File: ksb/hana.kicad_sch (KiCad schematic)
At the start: 20 parts, among them Q6 Q_PNP, U4 X850744-001

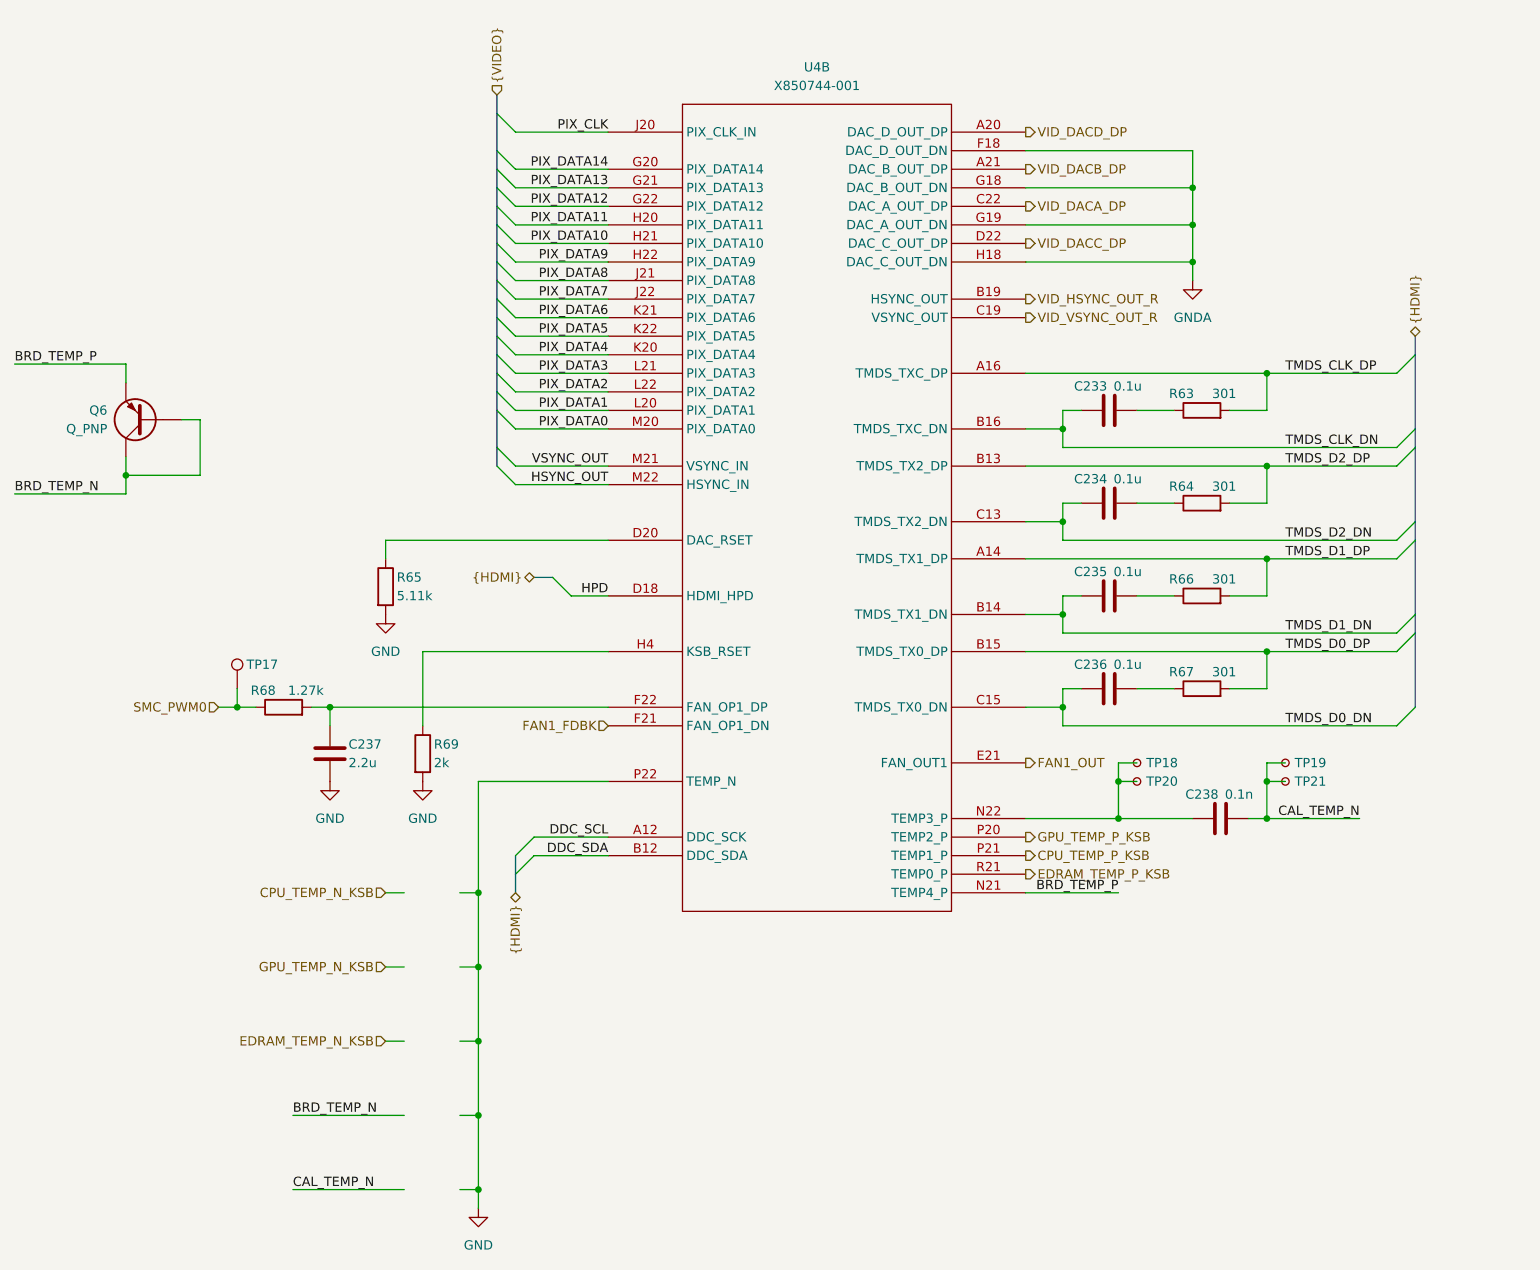
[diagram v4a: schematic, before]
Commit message: Nand Flash, Sata Connectors and removing (hopefully) unnecessary things
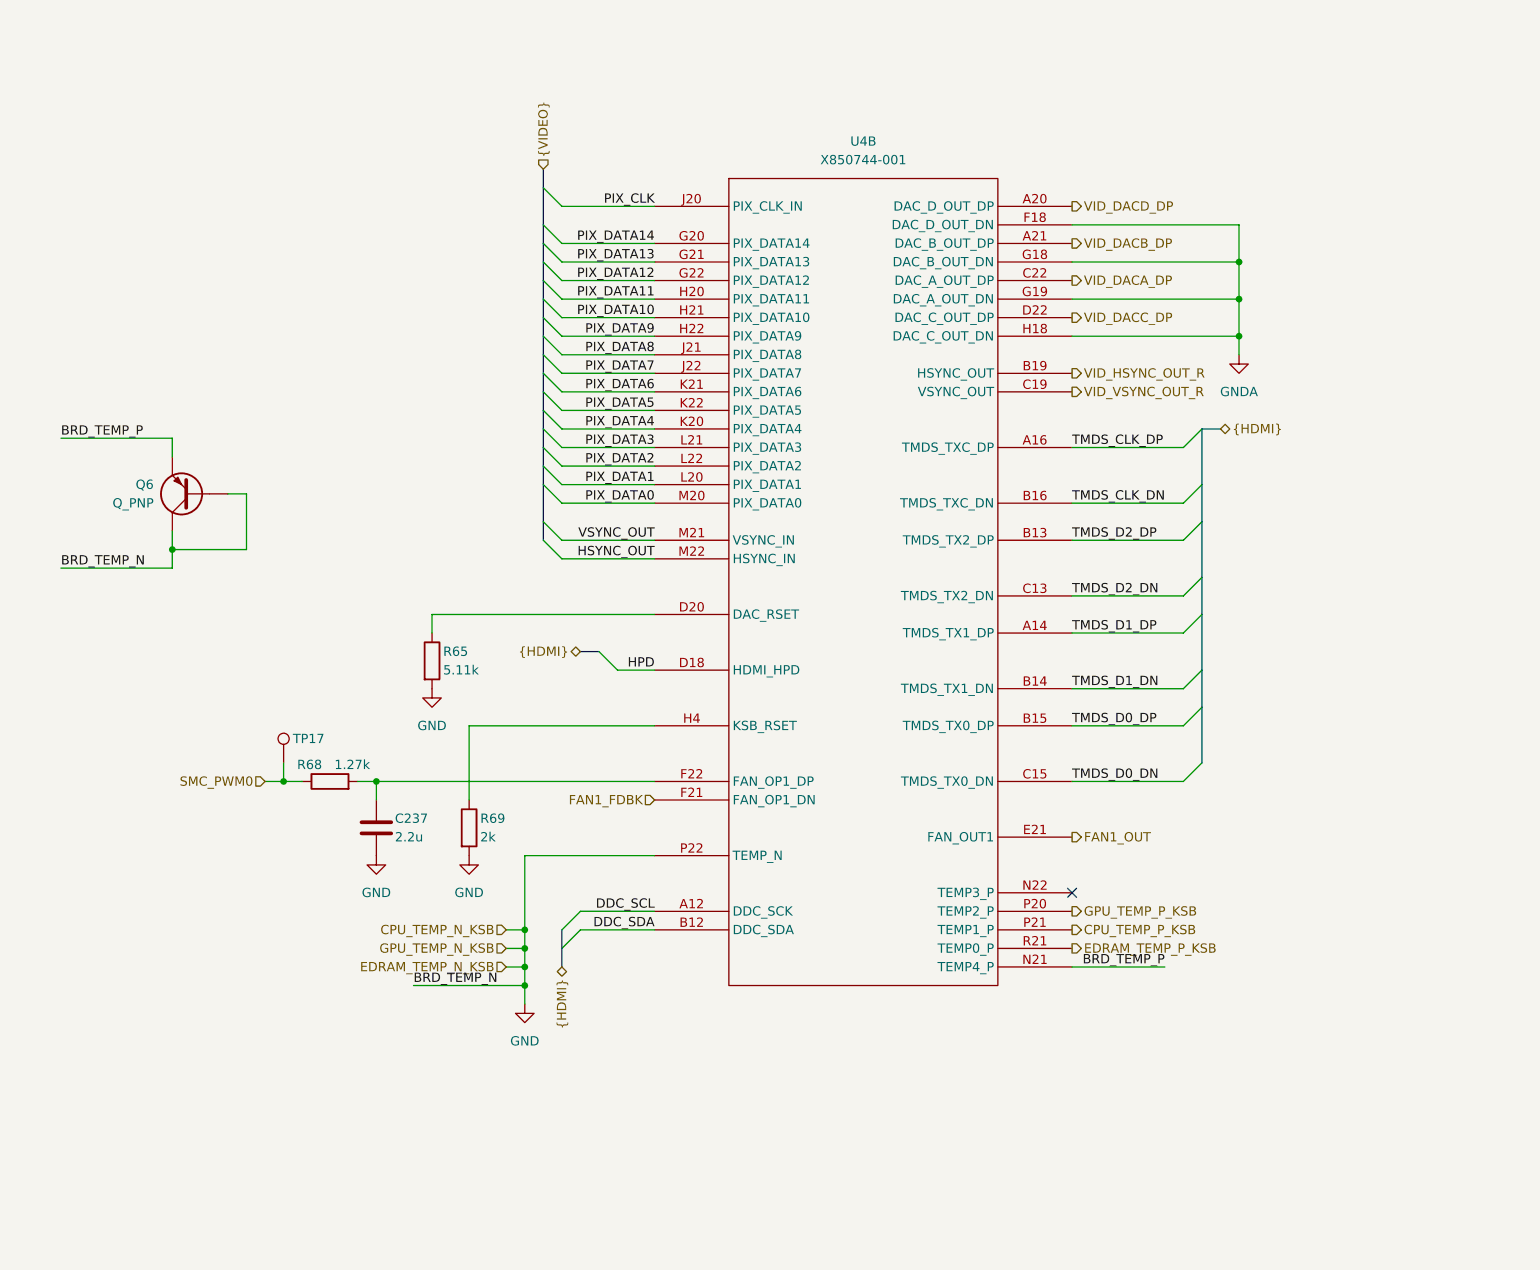
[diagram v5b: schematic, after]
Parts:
- removed C233, C234, C235, C236: 0.1u, symbol Device:C
- removed C238: 0.1n, symbol Device:C
- removed R63, R64, R66, R67: 301, symbol Device:R
- removed TP18, TP19, TP20, TP21: TestPoint_Small, symbol Connector:TestPoint_Small
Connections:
- net BRD_TEMP_N is gone; now on net GND: Q6.B, Q6.C
- no-connect marks 0 -> 1
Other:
- moved on the sheet: C237, Q6, R65, R68, R69, TP17, U4B

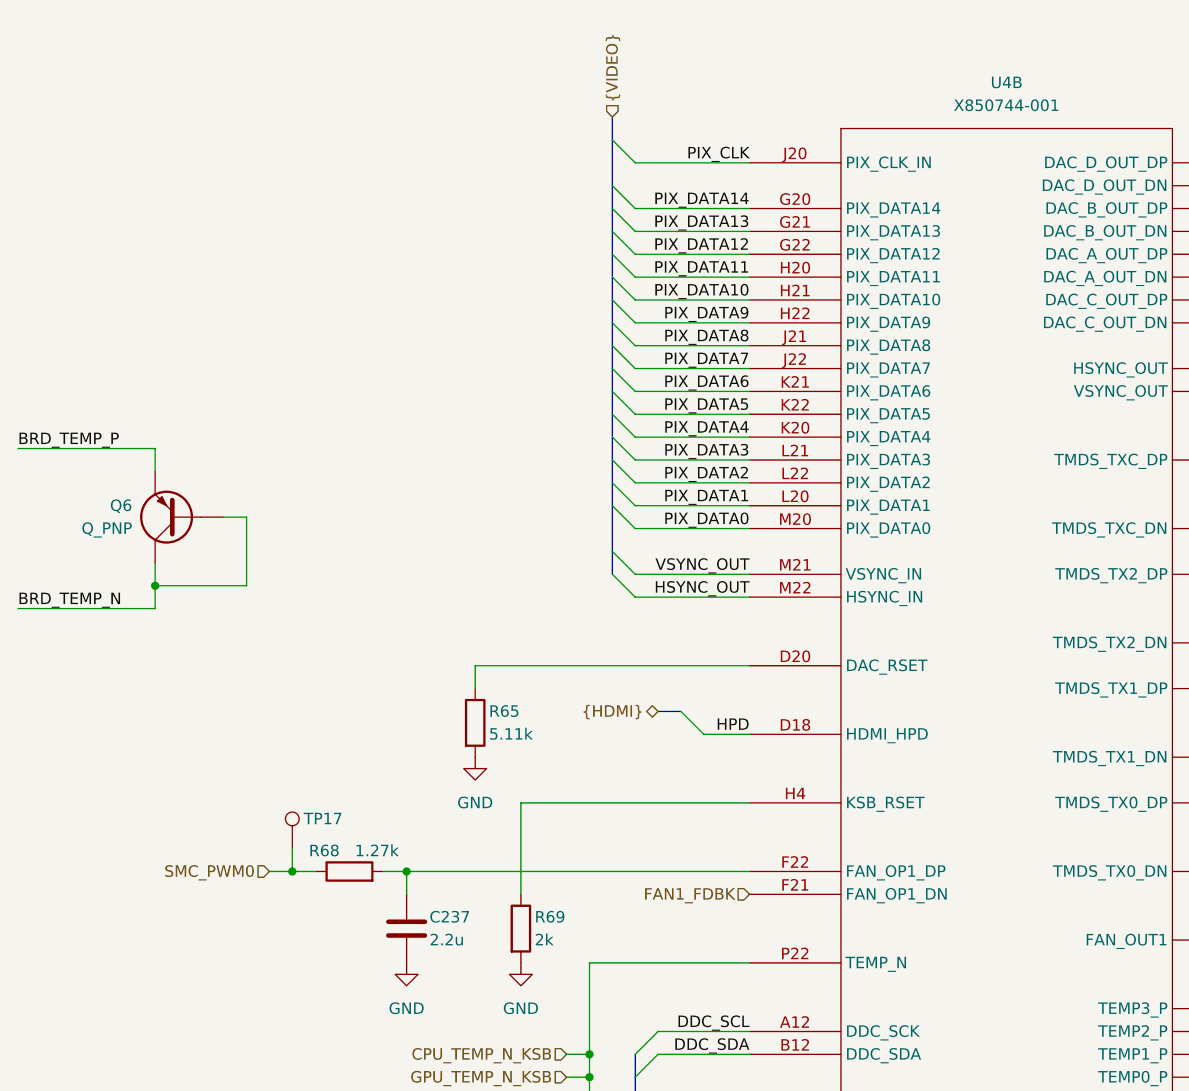
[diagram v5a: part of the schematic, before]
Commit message: Multipurpose and standby power rails, Reannotated schematic
Added V_1P2, V_1P8, V_5P0DUAL, V_EFUSE, V_GPUPCIE, V_3P3STBY and V_1P2STBY
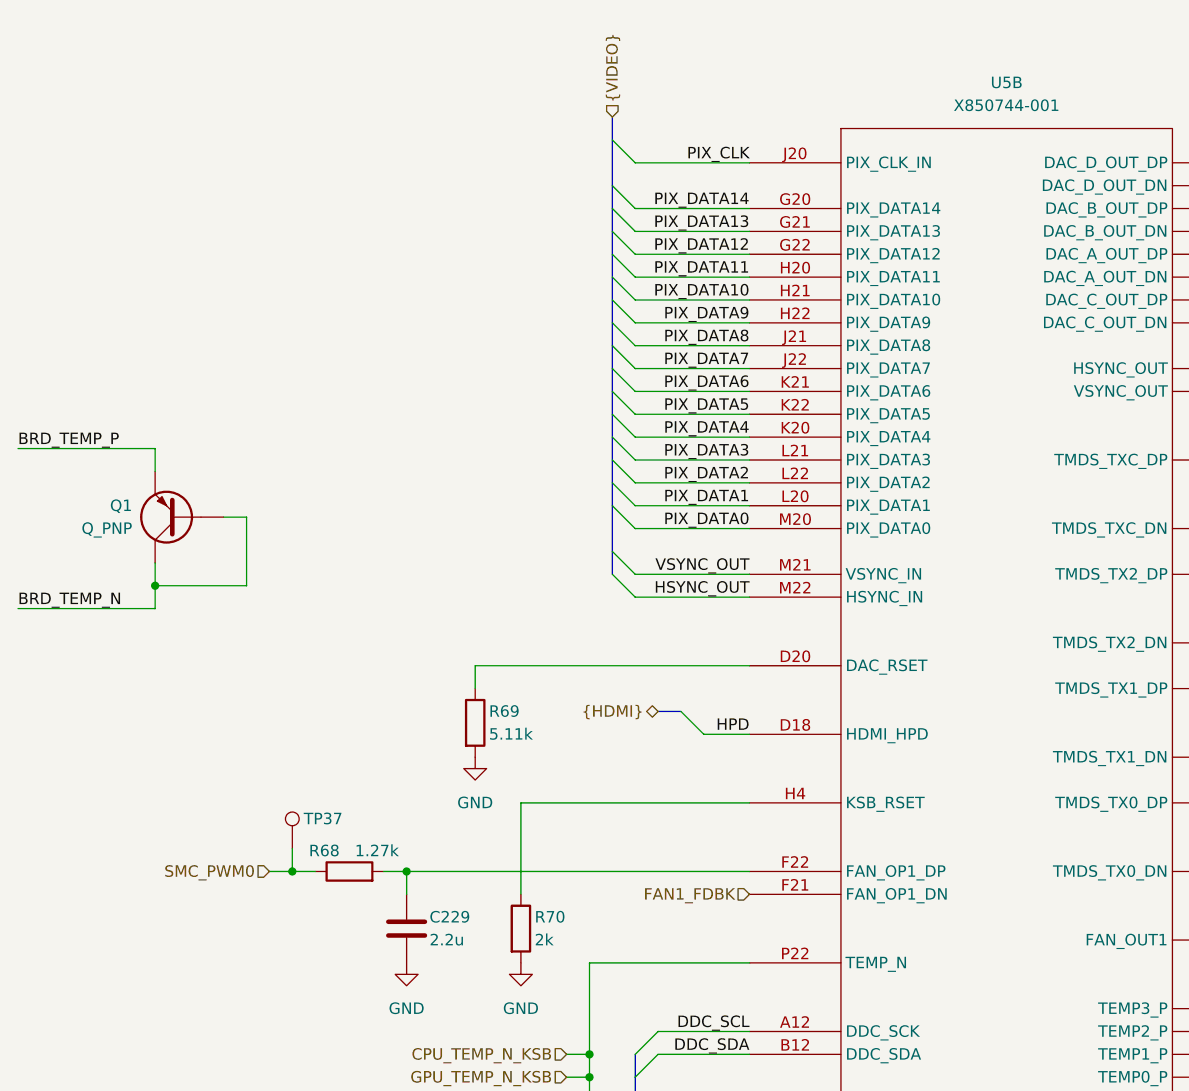
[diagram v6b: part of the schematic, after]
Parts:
- renumbered C237 to C229, Q6 to Q1, R65 to R69, R69 to R70, TP17 to TP37, U4 to U5
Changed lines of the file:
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@@
 		(dnp no)
 		(fields_autoplaced yes)
-		(property "Reference" "#PWR0109"
+		(property "Reference" "#PWR0108"
 			(at 100.33 138.43 0)
 			(effects
@@
 			(project "StingBurst"
 				(path "/16640ecb-e4a4-4594-871b-70047bfba6e0/5578fb0d-7a85-48a3-97bd-11e67ac7c8dc/d6113545-4299-4788-b32a-3a696a198c82"
-					(reference "#PWR0109")
+					(reference "#PWR0108")
 					(unit 1)
 				)
@@
 		(on_board yes)
 		(dnp no)
-		(property "Reference" "Q6"
+		(property "Reference" "Q1"
 			(at 57.15 81.28 0)
 			(effects
@@
 			(project "Mantaray"
 				(path "/16640ecb-e4a4-4594-871b-70047bfba6e0/5578fb0d-7a85-48a3-97bd-11e67ac7c8dc/d6113545-4299-4788-b32a-3a696a198c82"
-					(reference "Q6")
+					(reference "Q1")
 					(unit 1)
 				)
@@
 		(on_board yes)
 		(dnp no)
-		(property "Reference" "TP17"
+		(property "Reference" "TP37"
 			(at 76.2 116.078 0)
 			(effects
@@
 			(project "StingBurst"
 				(path "/16640ecb-e4a4-4594-871b-70047bfba6e0/5578fb0d-7a85-48a3-97bd-11e67ac7c8dc/d6113545-4299-4788-b32a-3a696a198c82"
-					(reference "TP17")
+					(reference "TP37")
 					(unit 1)
 				)
@@
 		(on_board yes)
 		(dnp no)
-		(property "Reference" "C237"
+		(property "Reference" "C229"
 			(at 90.17 127 0)
 			(effects
@@
 			(project "StingBurst"
 				(path "/16640ecb-e4a4-4594-871b-70047bfba6e0/5578fb0d-7a85-48a3-97bd-11e67ac7c8dc/d6113545-4299-4788-b32a-3a696a198c82"
-					(reference "C237")
+					(reference "C229")
 					(unit 1)
 				)
@@
 		(dnp no)
 		(fields_autoplaced yes)
-		(property "Reference" "#PWR0214"
+		(property "Reference" "#PWR0110"
 			(at 205.74 69.85 0)
 			(effects
@@
 			(project ""
 				(path "/16640ecb-e4a4-4594-871b-70047bfba6e0/5578fb0d-7a85-48a3-97bd-11e67ac7c8dc/d6113545-4299-4788-b32a-3a696a198c82"
-					(reference "#PWR0214")
+					(reference "#PWR0110")
 					(unit 1)
 				)
@@
 		(on_board yes)
 		(dnp no)
-		(property "Reference" "R69"
+		(property "Reference" "R70"
 			(at 101.854 127 0)
 			(effects
@@
 			(project "StingBurst"
 				(path "/16640ecb-e4a4-4594-871b-70047bfba6e0/5578fb0d-7a85-48a3-97bd-11e67ac7c8dc/d6113545-4299-4788-b32a-3a696a198c82"
-					(reference "R69")
+					(reference "R70")
 					(unit 1)
 				)
@@
 		(on_board yes)
 		(dnp no)
-		(property "Reference" "R65"
+		(property "Reference" "R69"
 			(at 96.774 104.14 0)
 			(effects
@@
 			(project "StingBurst"
 				(path "/16640ecb-e4a4-4594-871b-70047bfba6e0/5578fb0d-7a85-48a3-97bd-11e67ac7c8dc/d6113545-4299-4788-b32a-3a696a198c82"
-					(reference "R65")
+					(reference "R69")
 					(unit 1)
 				)
@@
 		(dnp no)
 		(fields_autoplaced yes)
-		(property "Reference" "#PWR0108"
+		(property "Reference" "#PWR0106"
 			(at 87.63 138.43 0)
 			(effects
@@
 			(project "StingBurst"
 				(path "/16640ecb-e4a4-4594-871b-70047bfba6e0/5578fb0d-7a85-48a3-97bd-11e67ac7c8dc/d6113545-4299-4788-b32a-3a696a198c82"
-					(reference "#PWR0108")
+					(reference "#PWR0106")
 					(unit 1)
 				)
@@
 		(dnp no)
 		(fields_autoplaced yes)
-		(property "Reference" "#PWR0110"
+		(property "Reference" "#PWR0109"
 			(at 107.95 158.75 0)
 			(effects
@@
 			(project "StingBurst"
 				(path "/16640ecb-e4a4-4594-871b-70047bfba6e0/5578fb0d-7a85-48a3-97bd-11e67ac7c8dc/d6113545-4299-4788-b32a-3a696a198c82"
-					(reference "#PWR0110")
+					(reference "#PWR0109")
 					(unit 1)
 				)
@@
 		(dnp no)
 		(fields_autoplaced yes)
-		(property "Reference" "U4"
+		(property "Reference" "U5"
 			(at 154.305 34.29 0)
 			(effects
@@
 			(project "StingBurst"
 				(path "/16640ecb-e4a4-4594-871b-70047bfba6e0/5578fb0d-7a85-48a3-97bd-11e67ac7c8dc/d6113545-4299-4788-b32a-3a696a198c82"
-					(reference "U4")
+					(reference "U5")
 					(unit 2)
 				)
